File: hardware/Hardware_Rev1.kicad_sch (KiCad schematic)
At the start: 43 parts, among them J1 RJ45_LED_Shielded, J2 6P6C, Q2 BUK9M9R5-40HX, U2 LT1910, U3 OKI, U5 TSR_1-2450, U6 Teensy4.1_DEV-16771

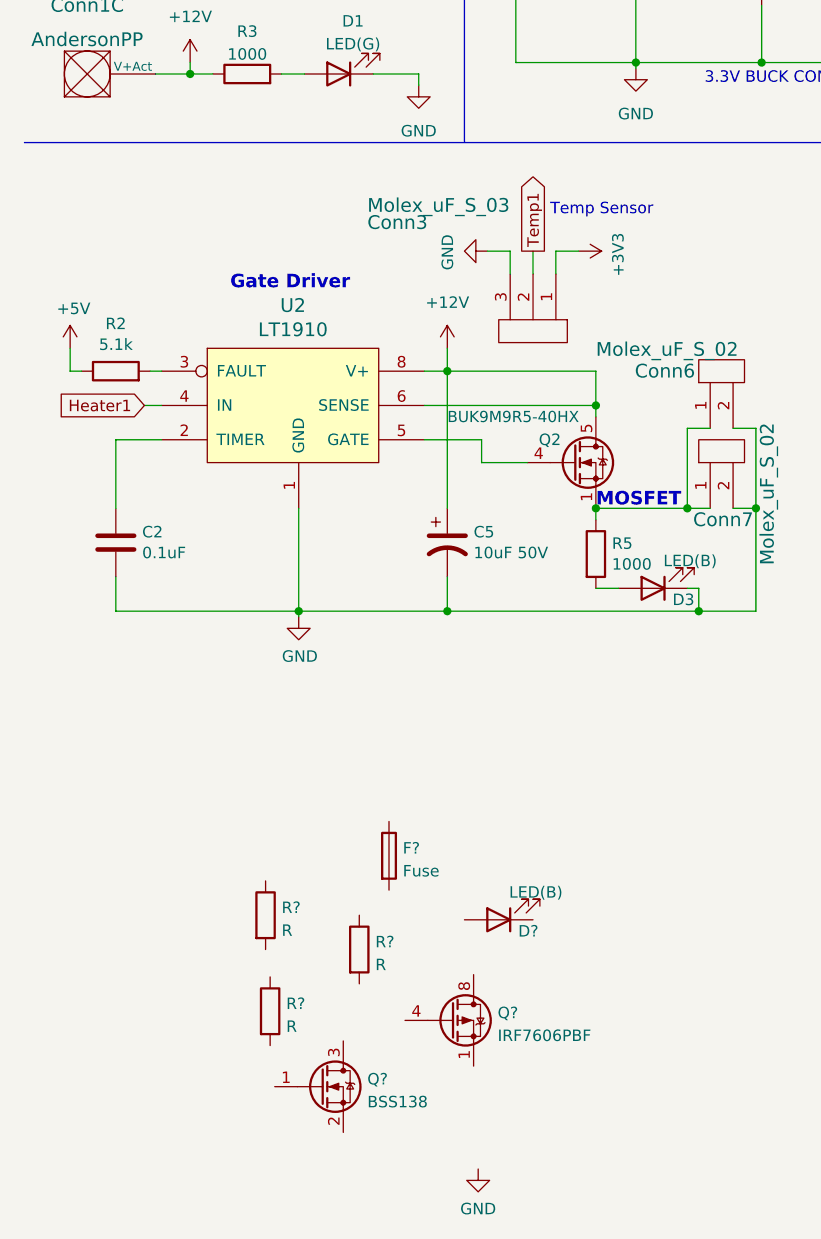
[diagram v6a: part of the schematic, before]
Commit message: just need to copy paste 11 more drive circuits and update the teensy
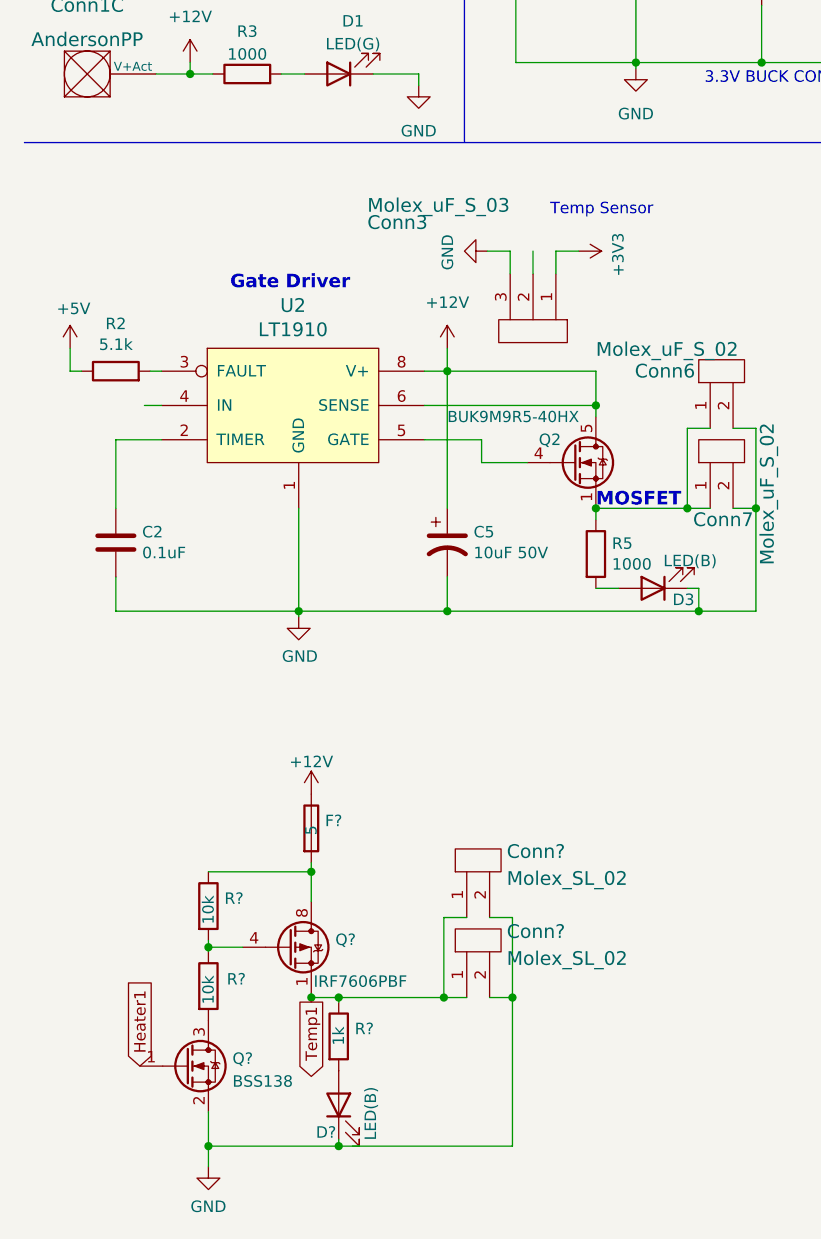
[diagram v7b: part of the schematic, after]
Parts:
- added Conn? (x2): Molex_SL_02, symbol MRDT_Connectors:Molex_SL_02
- F?: value Fuse -> 5
- R? (x2): value R -> 10k
- R?: value R -> 1k
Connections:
- net +12V: now also F?.1
- net GND: now also D?.1 (K), Q?.2 (S), Conn?.2, Conn?.2
- net Heater1: now also Q?.1 (G); no longer U2.4 (IN)
- net Temp1: now also Q?.1 (S), Q?.2 (S), Q?.3 (S), R?.1, Conn?.1, Conn?.1; no longer Conn3.2
- net at R?.1: now also Q?.4 (G), R?.2
- net at R?.2: now also Q?.3 (D)
- net at F?.2: now also Q?.5 (D), Q?.6 (D), Q?.7 (D), Q?.8 (D), R?.1
- net at R?.2: now also D?.2 (A)
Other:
- moved on the sheet: D?, F?, Q?, R?

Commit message: waht duh hek do I do for the teenser
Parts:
- removed C2: 0.1uF, Capacitor_SMD:C_0603_1608Metric_Pad1.08x0.95mm_HandSolder, symbol Device:C
- removed C5: 10uF 50V, Capacitor_SMD:C_0603_1608Metric_Pad1.08x0.95mm_HandSolder, symbol hardware-rescue:CP1-Device
- removed Conn3: Molex_uF_S_03, MRDT_Connectors:MOLEX_uF_S_03_Horizontal, symbol MRDT_Connectors:Molex_uF_S_03
- removed Conn6, Conn7: Molex_uF_S_02, MRDT_Connectors:MOLEX_uF_S_02_Horizontal, symbol MRDT_Connectors:Molex_uF_S_02
- removed D3: LED(B), LED_SMD:LED_0603_1608Metric_Pad1.05x0.95mm_HandSolder, symbol Device:LED
- removed Q2: BUK9M9R5-40HX, Package_TO_SOT_SMD:LFPAK33, symbol Transistor_FET:BUK7M33-60EX
- removed R2: 5.1k, Resistor_SMD:R_0603_1608Metric_Pad0.98x0.95mm_HandSolder, symbol Device:R
- removed R5: 1000, Resistor_SMD:R_0603_1608Metric_Pad0.98x0.95mm_HandSolder, symbol Device:R
- removed U2: LT1910, Package_SO:SOIC-8-N7_3.9x4.9mm_P1.27mm, symbol MRDT_ICs:LT1910
- added Conn? (x22): Molex_SL_02, symbol MRDT_Connectors:Molex_SL_02
- added D? (x11): LED(B), LED_SMD:LED_0603_1608Metric_Pad1.05x0.95mm_HandSolder, symbol Device:LED
- added F? (x11): 5, symbol Device:Fuse
- added Q? (x11): IRF7606PBF, Package_SO:MSOP-8_3x3mm_P0.65mm, symbol Transistor_FET:IRF7606PBF
- added Q? (x11): BSS138, Package_TO_SOT_SMD:SOT-23, symbol Transistor_FET:BSS138
- added R? (x11): 1k, symbol Device:R
- added R? (x22): 10k, symbol Device:R
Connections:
- net +12V: now also F?.1, F?.1, F?.1, F?.1, F?.1, F?.1, F?.1, F?.1, F?.1, F?.1, F?.1
- net GND: now also Conn?.2, Conn?.2, Conn?.2, Conn?.2, Conn?.2, Conn?.2, Conn?.2, Conn?.2, Conn?.2, Conn?.2, Conn?.2, Conn?.2, Conn?.2, Conn?.2, Conn?.2, Conn?.2, Conn?.2, Conn?.2, Conn?.2, Conn?.2, Conn?.2, Conn?.2, D?.1 (K), D?.1 (K), D?.1 (K), D?.1 (K), D?.1 (K), D?.1 (K), D?.1 (K), D?.1 (K), D?.1 (K), D?.1 (K), D?.1 (K), Q?.2 (S), Q?.2 (S), Q?.2 (S), Q?.2 (S), Q?.2 (S), Q?.2 (S), Q?.2 (S), Q?.2 (S), Q?.2 (S), Q?.2 (S), Q?.2 (S)
- net Heater2: now also Q?.1 (G)
- net Heater3: now also Q?.1 (G)
- net Temp2: now also Conn?.1, Conn?.1, Q?.1 (S), Q?.2 (S), Q?.3 (S), R?.1
- net Temp3: now also Conn?.1, Conn?.1, Q?.1 (S), Q?.2 (S), Q?.3 (S), R?.1
- net Temp4: now reaches U6.17 (A3)
- net Temp4: now also Conn?.1, Conn?.1, Q?.1 (S), Q?.2 (S), Q?.3 (S), R?.1
- net Temp5: now reaches U6.18 (A4)
- net Temp5: now also Conn?.1, Conn?.1, Q?.1 (S), Q?.2 (S), Q?.3 (S), R?.1
- net Temp6: now reaches U6.19 (A5)
- net Temp6: now also Conn?.1, Conn?.1, Q?.1 (S), Q?.2 (S), Q?.3 (S), R?.1
- net Temp7: now reaches U6.20 (A6)
- net Temp7: now also Conn?.1, Conn?.1, Q?.1 (S), Q?.2 (S), Q?.3 (S), R?.1
- net Temp8: now reaches U6.21 (A7)
- net Temp8: now also Conn?.1, Conn?.1, Q?.1 (S), Q?.2 (S), Q?.3 (S), R?.1
- net Temp9: now reaches U6.22 (A8)
- net Temp9: now also Conn?.1, Conn?.1, Q?.1 (S), Q?.2 (S), Q?.3 (S), R?.1
- net Temp12: now reaches U6.39 (A15)
- net Temp12: now also Conn?.1, Conn?.1, Q?.1 (S), Q?.2 (S), Q?.3 (S), R?.1
- net Temp11: now reaches U6.40 (A16)
- net Temp11: now also Conn?.1, Conn?.1, Q?.1 (S), Q?.2 (S), Q?.3 (S), R?.1
- net Temp10: now reaches U6.41 (A17)
- net Temp10: now also Conn?.1, Conn?.1, Q?.1 (S), Q?.2 (S), Q?.3 (S), R?.1
- new net: D?.2 (A), R?.2 (x11)
- new net: Q?.4 (G), R?.1, R?.2 (x11)
- new net: F?.2, Q?.5 (D), Q?.6 (D), Q?.7 (D), Q?.8 (D), R?.1 (x11)
- new net: Q?.3 (D), R?.2 (x11)
- new net Heater10: Q?.1 (G)
- new net Heater11: Q?.1 (G)
- new net Heater12: Q?.1 (G)
- new net Heater4: Q?.1 (G)
- new net Heater5: Q?.1 (G)
- new net Heater6: Q?.1 (G)
- new net Heater7: Q?.1 (G)
- new net Heater8: Q?.1 (G)
- new net Heater9: Q?.1 (G)
- no-connect marks 49 -> 40
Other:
- note added: "Vias :)"
- note removed: "Gate Driver"
- note removed: "MOSFET"
- note removed: "Temp Sensor"
- company: Jacob Byers, James Elverson, Joshua Perkins -> Jacob Byers, Joshua Perkins
- title: Water Heater Board - Rev1 -> Water Heater Board - Rev2?
- moved on the sheet: Conn?, D?, F?, Q?, R?, V1, V2, V3, V4
